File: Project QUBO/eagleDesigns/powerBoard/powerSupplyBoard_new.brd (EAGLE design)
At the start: 152.4 x 101.6 mm, 146 parts

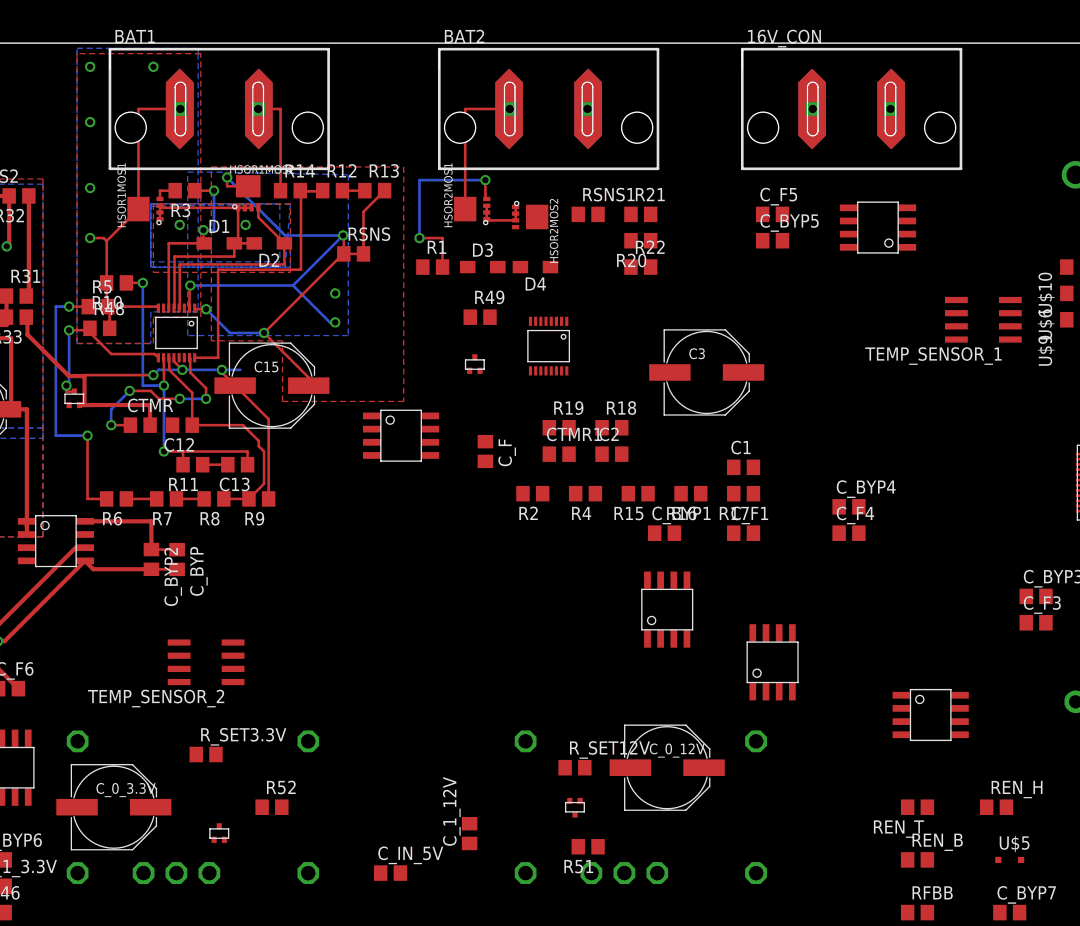
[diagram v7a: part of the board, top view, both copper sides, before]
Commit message: 
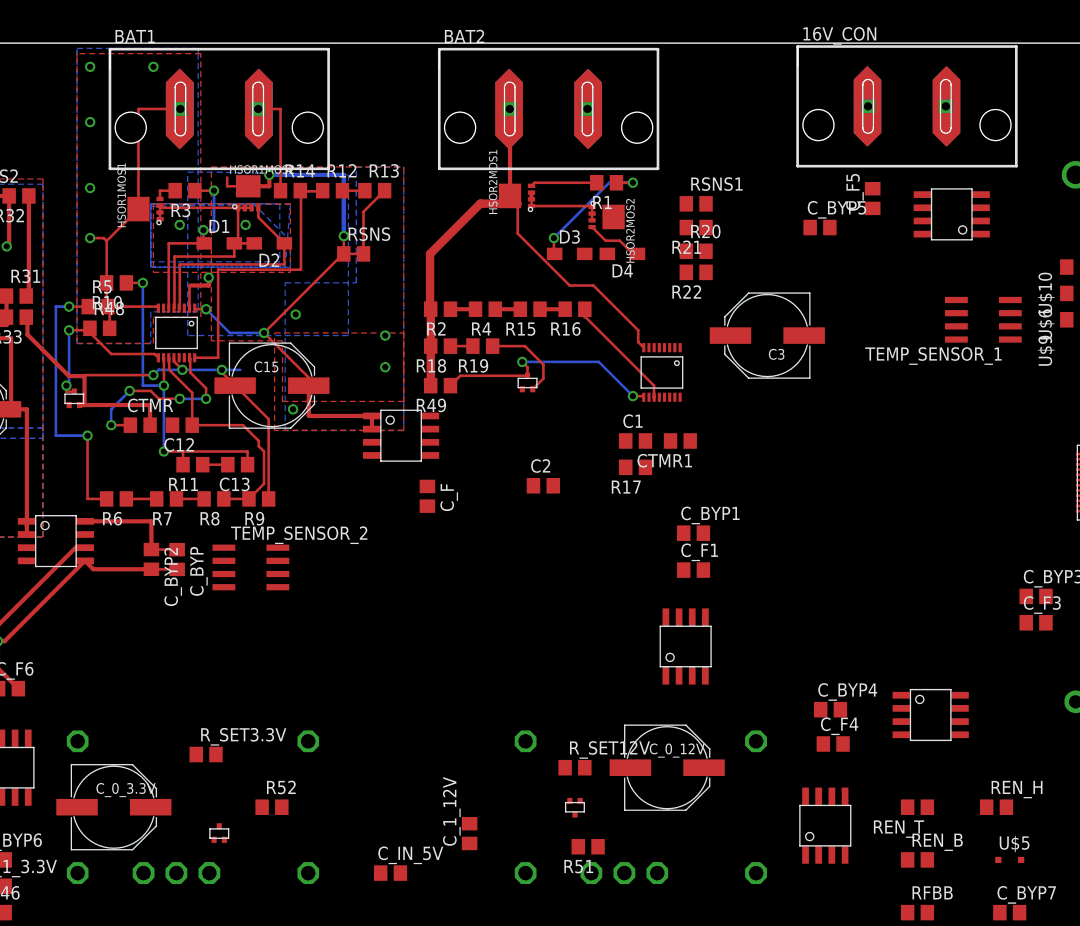
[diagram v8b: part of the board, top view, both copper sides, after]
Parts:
- moved R16 21.0 mm to (81.3, 75.9)
- moved R15 20.6 mm to (77.0, 75.9)
- moved C_F4 20.4 mm to (106.2, 34.0)
- moved R4 20.2 mm to (72.6, 75.9)
- moved R2 19.9 mm to (68.3, 75.9)
- moved C_BYP4 19.6 mm to (105.9, 37.3)
- moved R1 18.6 mm to (84.3, 88.1), turned to 180 degrees
- moved R18 18.3 mm to (68.3, 72.4), turned to 180 degrees
- moved 12VCS 16.5 mm to (105.4, 26.2)
- moved CTMR1 11.8 mm to (91.4, 63.2), turned to 180 degrees
- moved BAT2HSOR 11.2 mm to (89.7, 69.8)
- moved R19 10.8 mm to (72.4, 72.4), turned to 180 degrees
- moved R17 10.7 mm to (87.1, 60.7)
- moved C1 10.7 mm to (87.1, 63.2)
- moved RSNS1 10.5 mm to (93.0, 86.1)
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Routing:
- net BAT2: track 13.9 -> 52.9 mm
- net N$59: track 0.00 -> 22.5 mm, vias 0 -> 2
- net N$1: track 42.7 -> 25.7 mm, vias 5 -> 3
- net N$2: track 0.00 -> 13.0 mm, vias 0 -> 2
- net N$28: track 18.9 -> 6.41 mm, vias 2 -> 0
- net N$19: track 0.00 -> 11.3 mm
- net BAT1HSOROUT: track 34.2 -> 44.5 mm, vias 2 -> 6
- net GND: track 159.1 -> 167.5 mm
- net N$4: track 0.00 -> 5.44 mm
- net N$27: track 5.50 -> 8.47 mm
- net N$6: track 0.00 -> 2.42 mm
- net N$10: track 0.00 -> 2.42 mm
- net N$18: track 0.00 -> 2.42 mm
- net N$21: track 0.00 -> 2.16 mm
- added copper zone on layer 16, net BAT1HSOROUT
